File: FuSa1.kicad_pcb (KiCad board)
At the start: 4 copper layers, 78.5 x 87 mm, 114 parts, among them J1 XT60PW-M, J2 Conn_01x03_Pin, J20 ESC_HEADER, J21 SERVO_HEADER, J3 DC_JACK_5.5x2.1, J40 OLED_I2C, J50 I2C_EXP, J51 UART2_DEBUG, J53 NRF24_PA_LNA, J56 Screw_Terminal_01x03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

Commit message: 3D views
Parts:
- D30: moved to B.Cu
- moved TP3 8.63 mm to (76.0, 122.5)
- moved JP1 7.01 mm to (113.8, 87.5), turned to -90 degrees
- moved R75 3.19 mm to (112.0, 84.2), turned to -90 degrees
- moved D30 1.51 mm to (108.1, 82.5), turned to 180 degrees
- moved C70 0.87 mm to (105.0, 80.2), turned to -90 degrees
- moved C71 0.84 mm to (105.0, 83.3), turned to 90 degrees
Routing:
- net Net-(J56-Pin_3): track 24.0 -> 29.6 mm, vias 0 -> 1
- net Net-(D30-A1): track 2.18 -> 4.89 mm, vias 0 -> 1
- net Net-(D30-A2): track 2.00 -> 4.23 mm, vias 0 -> 1
- net /3_Motor_ESC_Control/5V_SERVO_CLEAN: track 12.6 -> 11.1 mm
- net /2_STM32_Module_Interface/3V3_MODULE: track 92.2 -> 91.2 mm
- net Net-(JP1-Pin_2): track 4.45 -> 3.55 mm
- net Net-(J56-Pin_2): track 22.5 -> 21.7 mm
- net /4_User_Interface/3V3_OUT: track 8.93 -> 9.73 mm
- net Net-(J2-Pin_2): track 22.8 -> 23.4 mm

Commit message: Updated BOM. Initial review and corrections
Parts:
- added REF**: MountingHole_3.2mm_M3_Pad, MountingHole:MountingHole_3.2mm_M3_Pad, F.Cu at (124.5, 63.0)
- added REF**: MountingHole_3.2mm_M3_Pad, MountingHole:MountingHole_3.2mm_M3_Pad, F.Cu at (54.0, 146.0)
- added REF**: MountingHole_3.2mm_M3_Pad, MountingHole:MountingHole_3.2mm_M3_Pad, F.Cu at (54.0, 63.0)
- added REF**: MountingHole_3.2mm_M3_Pad, MountingHole:MountingHole_3.2mm_M3_Pad, F.Cu at (124.5, 146.0)
- C10, C14, C48, C63: value 10uF -> 10uF/25V
- C11, C12, C13, C15, C40, C41, C42, C43, C44, C45, C49, C64, C7, C70, C71, C72, C74: value 0.1uF -> 100nF/50V
- C2, C4: value 100nF/25V -> 100nF/50V
- C32: footprint Capacitor_SMD:C_0805_2012Metric -> Capacitor_THT:CP_Radial_D5.0mm_P2.00mm
- C33: value 10uF -> 10uF/25V; moved to B.Cu
- F1: footprint Fuse:Fuse_1812_4532Metric -> Fuse:Fuse_1206_3216Metric
- moved J20 8.06 mm to (116.9, 139.0)
- moved C32 3.54 mm to (89.5, 139.0)
- moved C1 3.00 mm to (80.5, 95.0)
- moved C10 3.00 mm to (83.5, 124.3)
- moved C11 3.00 mm to (85.2, 124.4)
- moved C13 3.00 mm to (85.2, 130.4)
- moved C14 3.00 mm to (112.5, 127.3)
- moved C15 3.00 mm to (85.0, 101.3)
- moved C2 3.00 mm to (71.7, 94.2)
- moved C20 3.00 mm to (85.0, 97.2)
- moved C3 3.00 mm to (78.0, 140.3)
- moved C30 3.00 mm to (109.2, 136.0)
- moved C31 3.00 mm to (98.7, 136.0)
- moved C33 3.00 mm to (90.2, 141.5)
- moved C4 3.00 mm to (80.2, 137.0)
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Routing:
- net Net-(J56-Pin_3): track 29.6 -> 28.7 mm
- net /1_Power_Management/VBAT_PROTECTED: track 2.79 -> 3.53 mm
- net /2_STM32_Module_Interface/PWM_ESC: track 20.3 -> 20.9 mm
- net /3_Motor_ESC_Control/5V_SERVO_CLEAN: track 11.1 -> 11.7 mm, vias 0 -> 1
- net /1_Power_Management/GND: vias 49 -> 48
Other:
- board size 78.5 x 87 mm -> 78.5 x 91 mm

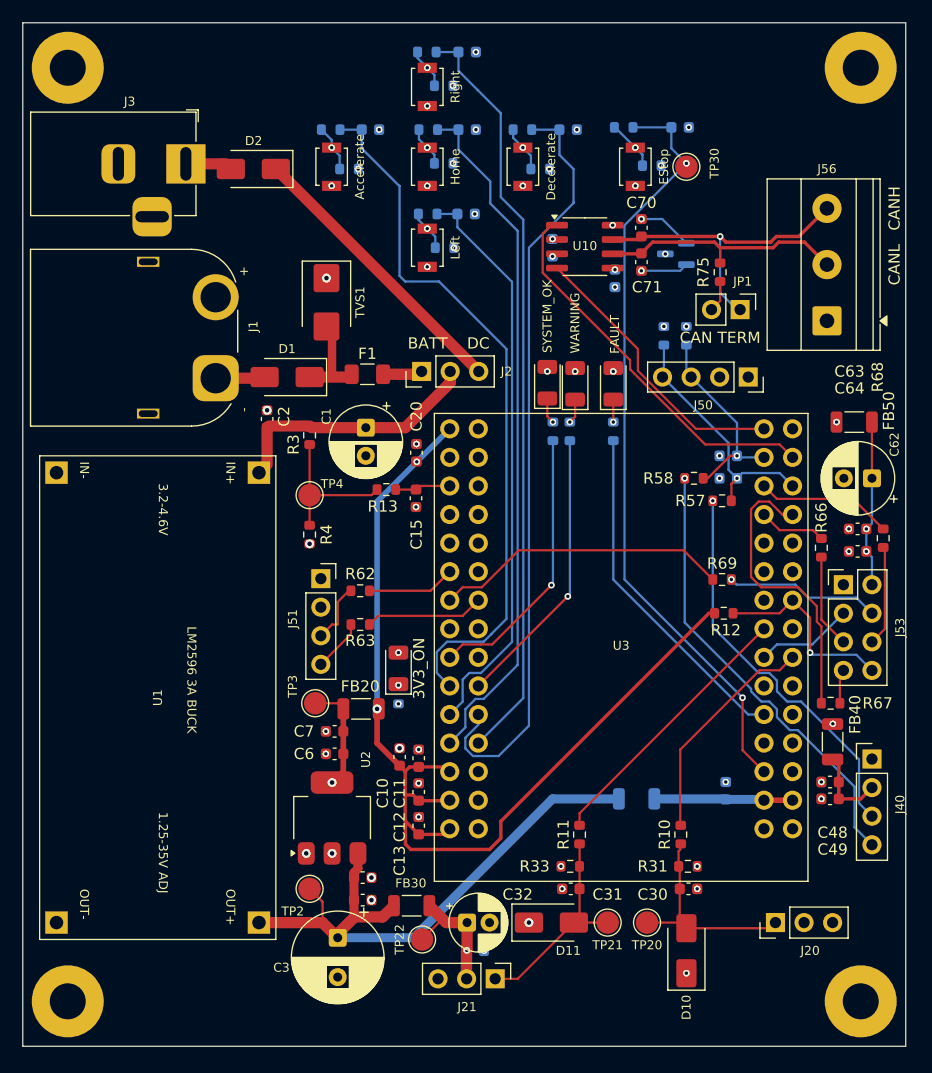
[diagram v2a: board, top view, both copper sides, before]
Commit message: Cleaned up schematic. Added mounting holes.
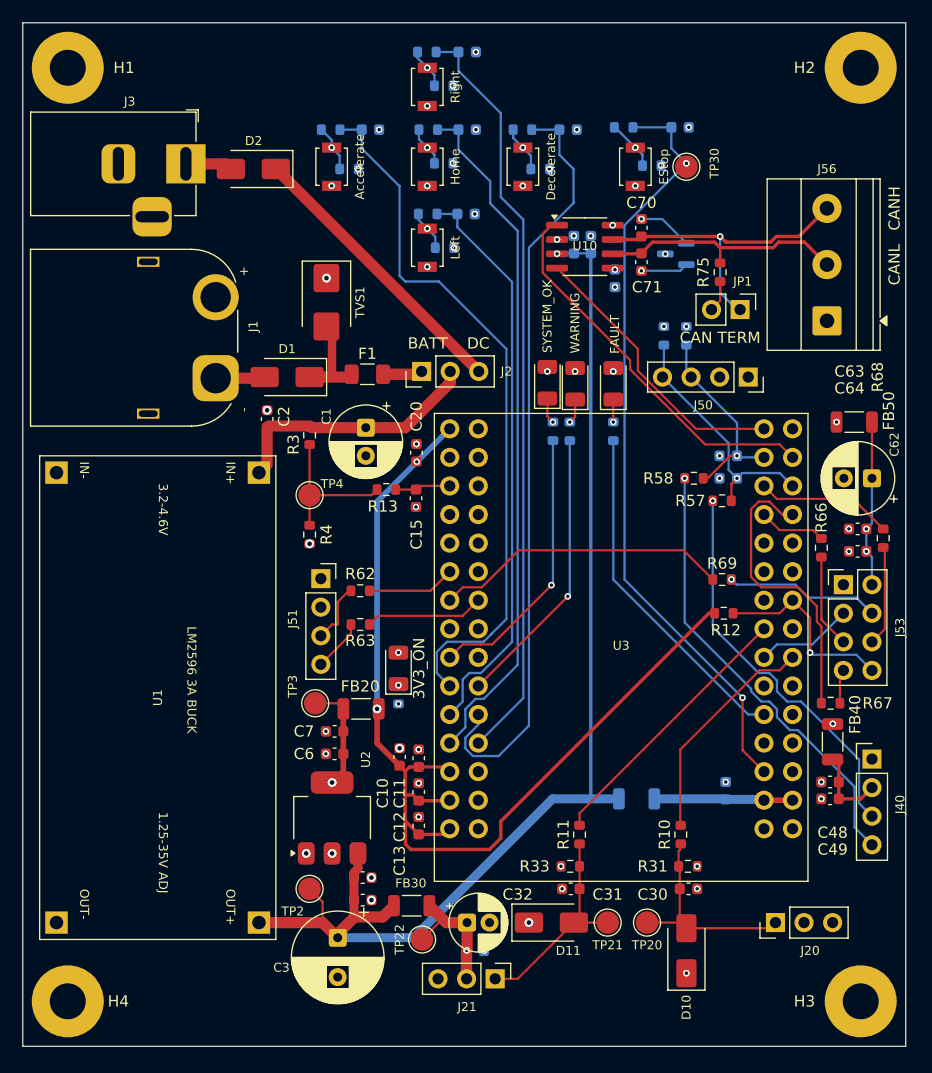
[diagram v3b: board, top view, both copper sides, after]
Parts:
- removed REF** (x4): MountingHole_3.2mm_M3_Pad, MountingHole:MountingHole_3.2mm_M3_Pad
- added C73: 100nF/50V, Capacitor_SMD:C_0603_1608Metric, B.Cu at (99.0, 78.7)
- added H1: MountingHole_Pad, MountingHole:MountingHole_3.2mm_M3_Pad, F.Cu at (54.0, 63.0)
- added H2: MountingHole_Pad, MountingHole:MountingHole_3.2mm_M3_Pad, F.Cu at (124.5, 63.0)
- added H3: MountingHole_Pad, MountingHole:MountingHole_3.2mm_M3_Pad, F.Cu at (124.5, 146.0)
- added H4: MountingHole_Pad, MountingHole:MountingHole_3.2mm_M3_Pad, F.Cu at (54.0, 146.0)
- C72: value 100nF/50V -> 4.7uF/25V
- moved C72 3.41 mm to (100.5, 78.7), turned to -90 degrees
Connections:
- C72 pad 1: /4_User_Interface/3V3_OUT -> /1_Power_Management/GND
- C72 pad 2: /1_Power_Management/GND -> /1_Power_Management/5V_BUCK
- U10 pad 3: /4_User_Interface/3V3_OUT -> /1_Power_Management/5V_BUCK
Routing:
- net /1_Power_Management/5V_BUCK: track 53.7 -> 105.2 mm, vias 0 -> 1
- net /4_User_Interface/3V3_OUT: vias 15 -> 14
- net /1_Power_Management/GND: vias 48 -> 50
